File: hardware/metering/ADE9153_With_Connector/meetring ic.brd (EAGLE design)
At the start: 134.3 x 92.7 mm, 38 parts, among them J9 AK300/2-5,0-GRAU, Y1 12.288mhz

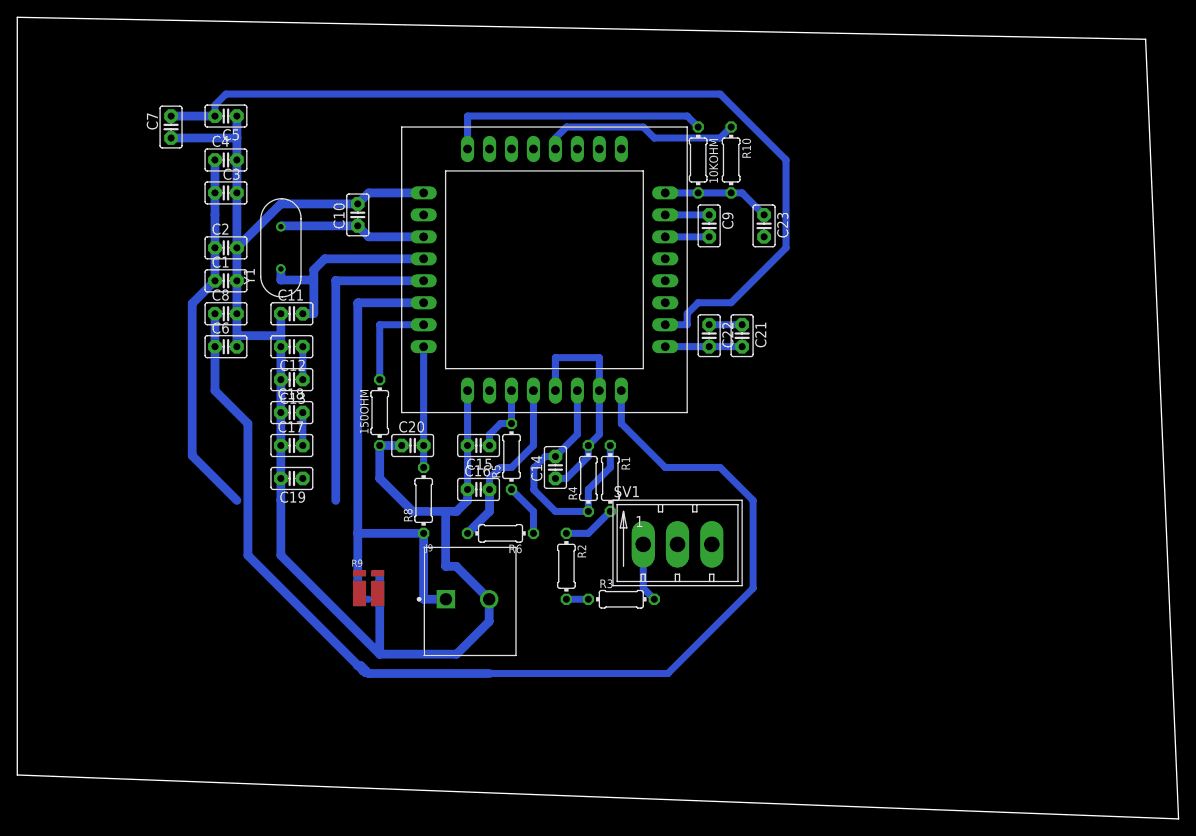
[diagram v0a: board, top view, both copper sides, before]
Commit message: change in metering IC design
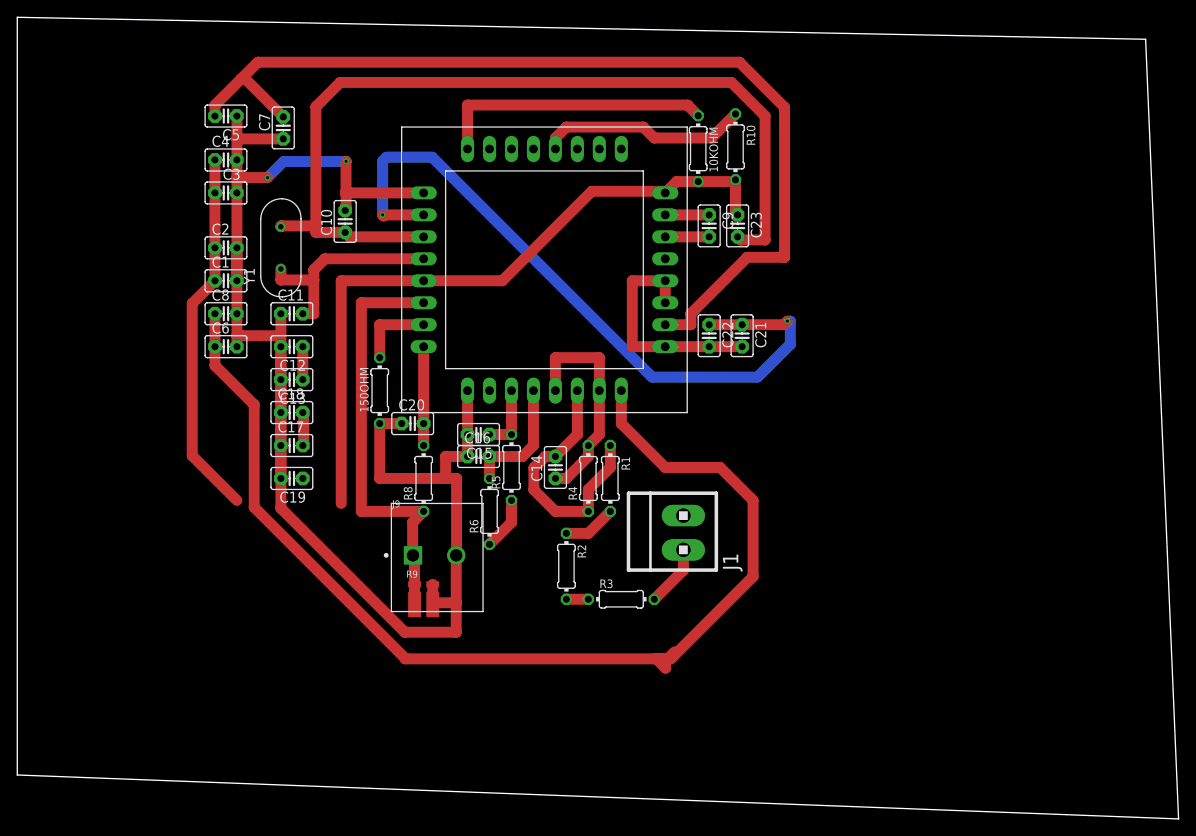
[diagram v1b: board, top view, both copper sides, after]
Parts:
- removed SV1: (no value), con-amp-mt6:MT6-3
- added J1: (no value), con-amp:1X2MTA
- moved C7 13.0 mm to (42.2, 24.0)
- moved R9 6.48 mm to (58.4, -30.5)
- moved J9 6.35 mm to (59.7, -25.4)
- moved C16 3.81 mm to (64.8, -14.0)
- moved C23 3.06 mm to (94.7, 12.7)
- moved R6 2.84 mm to (66.0, -20.3), turned to 90 degrees
- moved 150OHM 2.54 mm to (53.3, -6.35)
- moved C20 2.54 mm to (57.1, -10.2)
- moved R8 2.54 mm to (58.4, -16.5)
- moved C10 1.64 mm to (49.3, 13.2)
- moved R10 1.59 mm to (94.5, 21.8)
- moved 10KOHM 1.31 mm to (90.2, 21.6)
- moved C15 1.27 mm to (64.8, -11.4)
- moved R5 1.27 mm to (68.6, -15.2)
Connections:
- net N$27: now also J1.2; no longer SV1.1
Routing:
- net N$8: track 17.2 -> 103.8 mm
- net N$22: track 3.81 -> 82.7 mm, vias 0 -> 2
- net N$3: track 160.1 -> 128.6 mm
- net GND: track 233.5 -> 213.2 mm, vias 0 -> 2
- net 3V3: track 103.4 -> 123.1 mm
- net N$24: track 60.9 -> 49.9 mm
- net N$4: track 104.6 -> 113.2 mm
- net N$15: track 20.4 -> 14.5 mm
- net N$7: track 28.5 -> 24.7 mm
- net N$21: track 14.0 -> 11.4 mm
- net N$20: track 11.4 -> 8.89 mm
- net GPIO5: track 31.0 -> 32.3 mm
- net GPIO17: track 23.2 -> 24.3 mm
- net N$16: track 8.15 -> 7.62 mm

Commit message: files change
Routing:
- net N$9: track 3.81 -> 75.9 mm, vias 0 -> 1
- net GND: track 213.2 -> 275.3 mm, vias 2 -> 4
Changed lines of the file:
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@@
 <wire x1="63.5" y1="-6.35" x2="63.5" y2="-11.43" width="1.27" layer="1"/>
 <wire x1="63.5" y1="-11.43" x2="63.5" y2="-13.97" width="1.27" layer="1"/>
-<wire x1="86.36" y1="-1.27" x2="95.25" y2="-1.27" width="1.27" layer="1"/>
+<wire x1="86.36" y1="-1.27" x2="93.47829375" y2="-1.27" width="1.27" layer="1"/>
+<wire x1="93.47829375" y1="-1.27" x2="95.25" y2="-1.27" width="1.27" layer="1"/>
 <wire x1="36.83" y1="6.35" x2="36.83" y2="10.16" width="1.27" layer="1"/>
 <wire x1="49.345796875" y1="14.483175" x2="49.345796875" y2="14.82115" width="1.27" layer="1"/>
@@
 <wire x1="49.447371875" y1="14.922725" x2="49.345796875" y2="14.82115" width="1.27" layer="1"/>
 <wire x1="49.3898" y1="16.623084375" x2="49.3898" y2="16.51" width="1.27" layer="1"/>
+<wire x1="93.47829375" y1="-1.27" x2="93.981315625" y2="-1.773021875" width="1.27" layer="1"/>
+<wire x1="93.981315625" y1="-10.814453125" x2="94.148990625" y2="-10.982128125" width="1.27" layer="1"/>
+<via x="94.148990625" y="-10.982128125" extent="1-16" drill="0.35"/>
+<wire x1="94.148990625" y1="-10.982128125" x2="88.364509375" y2="-16.766609375" width="1.27" layer="16"/>
+<wire x1="88.364509375" y1="-16.766609375" x2="75.45333125" y2="-16.766609375" width="1.27" layer="16"/>
+<wire x1="75.45333125" y1="-16.766609375" x2="75.2475" y2="-16.972440625" width="1.27" layer="16"/>
+<wire x1="75.2475" y1="-16.972440625" x2="75.2475" y2="-17.16756875" width="1.27" layer="16"/>
+<wire x1="75.2475" y1="-17.16756875" x2="74.950309375" y2="-17.464759375" width="1.27" layer="16"/>
+<wire x1="74.950309375" y1="-17.464759375" x2="74.950309375" y2="-19.0301" width="1.27" layer="16"/>
+<wire x1="74.950309375" y1="-19.0301" x2="72.435315625" y2="-21.54509375" width="1.27" layer="16"/>
+<wire x1="72.435315625" y1="-21.54509375" x2="61.78789375" y2="-21.54509375" width="1.27" layer="16"/>
+<wire x1="61.78789375" y1="-21.54509375" x2="60.362665625" y2="-20.119865625" width="1.27" layer="16"/>
+<wire x1="60.362665625" y1="-20.119865625" x2="60.362665625" y2="-11.0659625" width="1.27" layer="16"/>
+<wire x1="60.362665625" y1="-11.0659625" x2="60.446503125" y2="-11.0659625" width="1.27" layer="16"/>
+<via x="60.446503125" y="-11.0659625" extent="1-16" drill="0.35"/>
+<wire x1="60.446503125" y1="-11.0659625" x2="63.1359625" y2="-11.0659625" width="1.27" layer="1"/>
+<wire x1="63.1359625" y1="-11.0659625" x2="63.5" y2="-11.43" width="1.27" layer="1"/>
+<wire x1="93.981315625" y1="-1.773021875" x2="93.981315625" y2="-10.814453125" width="1.27" layer="1"/>
 <wire x1="95.25" y1="-1.27" x2="91.44" y2="-1.27" width="0" layer="19" extent="1-1"/>
-<wire x1="63.5" y1="-6.35" x2="86.36" y2="-1.27" width="0" layer="19" extent="1-1"/>
+<wire x1="49.3898" y1="16.623084375" x2="49.345796875" y2="14.483175" width="0" layer="19" extent="1-1"/>
 <wire x1="36.83" y1="2.54" x2="36.83" y2="6.35" width="0" layer="19" extent="1-1"/>
 <wire x1="41.91" y1="-8.89" x2="41.91" y2="-5.08" width="0" layer="19" extent="1-1"/>
@@
 <contactref element="C13" pad="1"/>
 <wire x1="44.45" y1="-1.27" x2="44.45" y2="-5.08" width="1.27" layer="1"/>
-<wire x1="44.45" y1="-1.27" x2="86.36" y2="8.89" width="0" layer="19" extent="1-1"/>
+<wire x1="81.609840625" y1="8.3250875" x2="86.36" y2="8.89" width="0" layer="19" extent="1-1"/>
+<wire x1="44.45" y1="-1.27" x2="45.545346875" y2="-0.174653125" width="1.27" layer="1"/>
+<wire x1="45.545346875" y1="-0.174653125" x2="46.010965625" y2="-0.174653125" width="1.27" layer="1"/>
+<wire x1="46.010965625" y1="-0.174653125" x2="46.359875" y2="-0.174653125" width="1.27" layer="1"/>
+<wire x1="46.359875" y1="-0.174653125" x2="46.476309375" y2="-0.05821875" width="1.27" layer="1"/>
+<via x="46.476309375" y="-0.05821875" extent="1-16" drill="0.35"/>
+<wire x1="46.476309375" y1="-0.05821875" x2="51.94874375" y2="-5.530653125" width="1.27" layer="16"/>
+<wire x1="51.94874375" y1="-5.530653125" x2="54.387171875" y2="-5.530653125" width="1.27" layer="16"/>
+<wire x1="53.038859375" y1="21.550484375" x2="53.038859375" y2="21.550490625" width="1.27" layer="16"/>
+<wire x1="46.476309375" y1="-0.05821875" x2="46.476309375" y2="14.987934375" width="1.27" layer="16"/>
+<wire x1="46.476309375" y1="14.987934375" x2="53.038859375" y2="21.550484375" width="1.27" layer="16"/>
+<wire x1="53.038859375" y1="21.550490625" x2="53.843846875" y2="22.355478125" width="1.27" layer="16"/>
+<wire x1="53.843846875" y1="22.355478125" x2="60.378484375" y2="22.355478125" width="1.27" layer="16"/>
+<wire x1="61.9506" y1="20.1862125" x2="62.8582125" y2="19.2786" width="1.27" layer="16"/>
+<wire x1="66.4105" y1="19.2786" x2="76.84005625" y2="8.84904375" width="1.27" layer="16"/>
+<wire x1="60.378484375" y1="22.355478125" x2="61.9506" y2="20.7833625" width="1.27" layer="16"/>
+<wire x1="61.9506" y1="20.7833625" x2="61.9506" y2="20.1862125" width="1.27" layer="16"/>
+<wire x1="62.8582125" y1="19.2786" x2="66.4105" y2="19.2786" width="1.27" layer="16"/>
+<wire x1="76.84005625" y1="8.84904375" x2="77.3640125" y2="8.3250875" width="1.27" layer="16"/>
+<wire x1="77.3640125" y1="8.3250875" x2="81.609840625" y2="8.3250875" width="1.27" layer="16"/>
 </signal>
 <signal name="N$11">
